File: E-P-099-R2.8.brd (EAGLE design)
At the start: 100 x 80 mm, 86 parts, among them J1 AVR_ISP

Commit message: Gerbers Generated
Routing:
- net GND: track 4.96 -> 15.3 mm, vias 12 -> 17
- net +12V: track 11.4 -> 15.6 mm
- net MISO: track 38.6 -> 41.0 mm
- net N$43: track 23.0 -> 22.2 mm

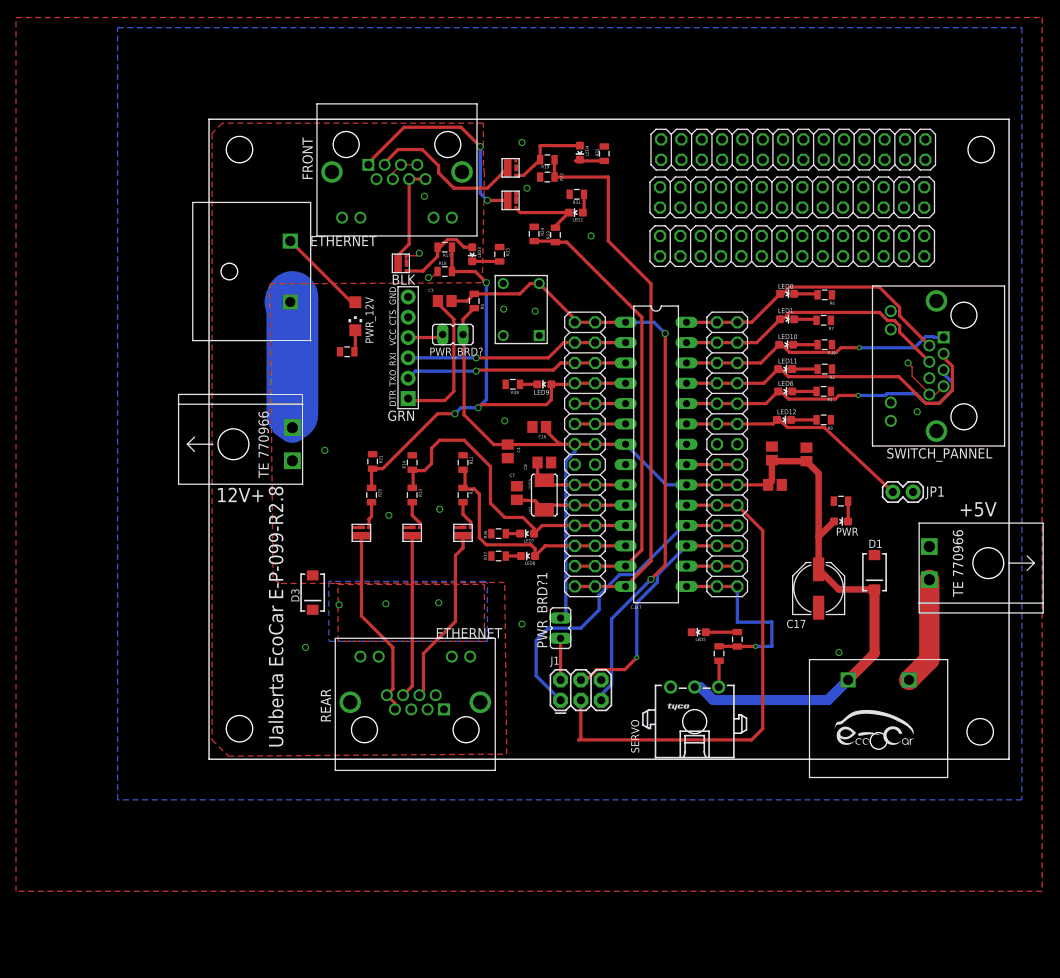
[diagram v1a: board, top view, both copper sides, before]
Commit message: VER.3
Added through hole mosfets, fixed input switch logic, improved pull downs on inout, added connector for break switch,   increased board size and fixed routing,
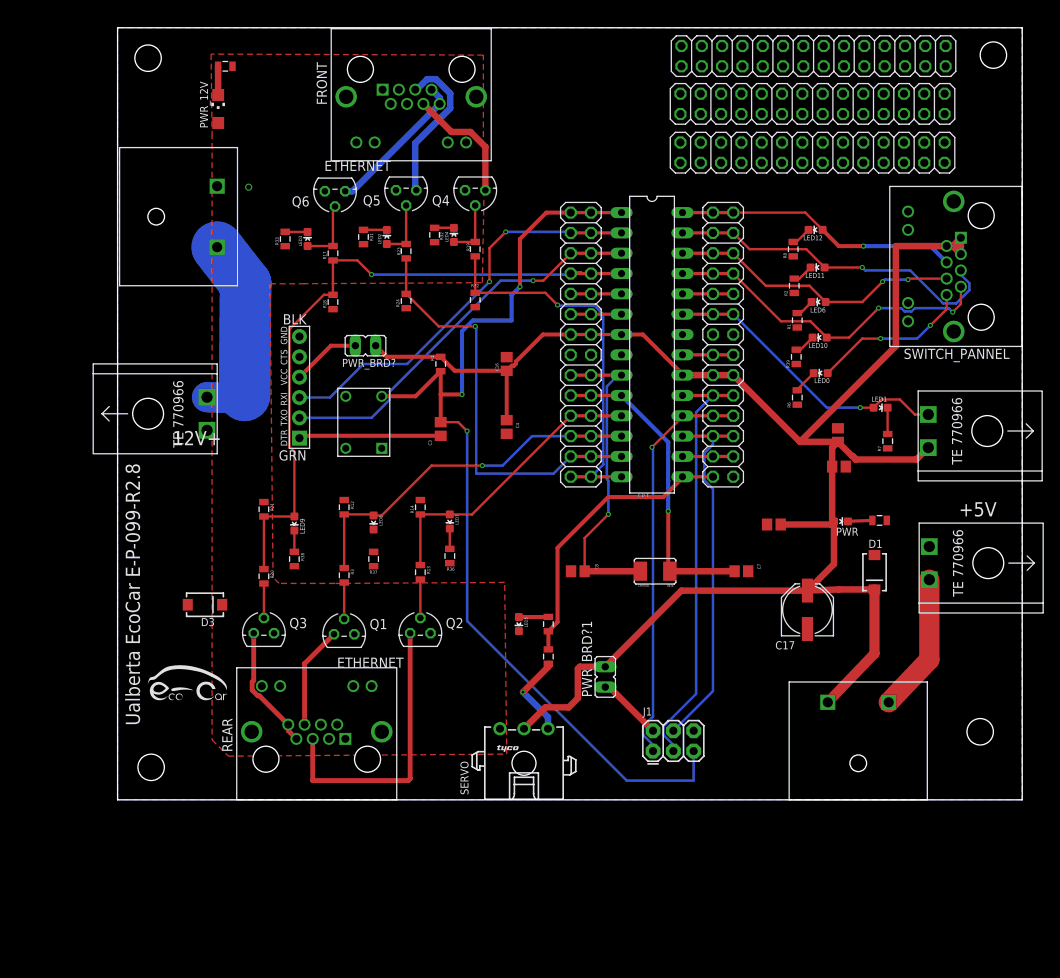
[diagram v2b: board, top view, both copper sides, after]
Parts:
- removed JP1: (no value), SparkFun-Retired:1X02
- removed U$10, U$11, U$13, U$14, U$15, U$20: SIA426DJ, Shell2013:SC70-6L
- added Q1, Q2, Q3, Q4, Q5, Q6: BSS101, transistor-fet:TO92
- added U$3: TE770966, Shell2013(1):2X1-MATE-N-LOCK
- moved R16 38.8 mm to (2.03, 86.6), turned to 0 degrees
- moved LED9 35.8 mm to (10.7, 29.5), turned to 180 degrees
- moved R38 35.0 mm to (10.7, 25.0), turned to 270 degrees
- moved PWR_12V 31.1 mm to (1.14, 81.3), turned to 0 degrees
- moved C7 29.7 mm to (66.5, 23.5), turned to 0 degrees
- moved R31 27.2 mm to (19.3, 65.3), turned to 90 degrees
- moved R33 26.9 mm to (9.53, 65.0), turned to 90 degrees
- moved U$12 24.2 mm to (21.6, 38.9)
- moved LED12 24.1 mm to (75.8, 66.2), turned to 90 degrees
- moved LED2 23.8 mm to (22.2, 65.3), turned to 0 degrees
- moved R34 23.7 mm to (42.4, 16.9)
- moved R32 23.5 mm to (28.2, 65.5), turned to 90 degrees
- moved LED5 22.5 mm to (38.7, 16.9), turned to 180 degrees
- moved SERVO 22.0 mm to (39.4, -0.51)
- moved R8 21.7 mm to (73.0, 63.8), turned to 90 degrees
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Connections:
- removed net N$27: FRONT.P$6, FRONT.P$8, U$10.D
- removed net N$43: REAR.P$4, U$14.D
- removed net N$49: LED2.A, R31.2
- new net N$14: Q2.2, R13.2
- new net N$15: Q1.2, R3.2
- new net N$22: FRONT.P$5, Q5.3
- net +12V: now also FRONT.P$1, FRONT.P$3, REAR.P$4; no longer FRONT.P$5, FRONT.P$7, REAR.P$5
- net +5V: now also SWITCH_PANNEL.P$1, SWITCH_PANNEL.P$2, SWITCH_PANNEL.P$3, U$3.CIRCUIT1
- net BREAK_SWITCH: now also LED1.A, U$3.CIRCUIT2; no longer JP1.1, LED12.A
- net DRIVING_LIGHTS_SWITCH: now also LED6.A, SWITCH_PANNEL.P$6; no longer LED10.A, SWITCH_PANNEL.P$1
- net FREE: now also LED0.A, SWITCH_PANNEL.P$8; no longer SWITCH_PANNEL.P$6
- net GND: now also Q1.1, Q2.1, Q3.1, Q4.1, Q5.1, Q6.1; no longer FRONT.P$13, FRONT.P$14, JP1.2, SWITCH_PANNEL.P$13, SWITCH_PANNEL.P$14, SWITCH_PANNEL.P$7, SWITCH_PANNEL.P$8, U$10.S@0, U$10.S@1, U$11.S@0, U$11.S@1, U$13.S@0, U$13.S@1, U$14.S@0, U$14.S@1, U$15.S@0, U$15.S@1, U$20.S@0, U$20.S@1
- net HAZ_SWITCH: now also LED10.A, SWITCH_PANNEL.P$7; no longer LED11.A, SWITCH_PANNEL.P$3
- net LEFT_SWITCH: now also LED11.A, SWITCH_PANNEL.P$5; no longer LED1.A, SWITCH_PANNEL.P$4
- net N$17: now also LED2.A, Q5.2; no longer LED2.C, U$20.G
- net N$20: now also FRONT.P$7, FRONT.P$8, Q6.3; no longer FRONT.P$1, U$20.D
- net N$21: now also FRONT.P$6, Q4.3; no longer R3.2, U$14.G
- net N$23: now also LED2.C, R31.2; no longer FRONT.P$3, U$11.D
- net N$33: now also Q4.2; no longer U$11.G
- net N$35: now also Q6.2; no longer U$10.G
- net N$4: now also Q3.3; no longer U$13.D
- net N$5: now also Q1.3; no longer U$15.D
- net N$7: now also Q2.3, REAR.P$5; no longer R13.2, U$15.G
- net N$8: now also Q3.2; no longer U$13.G
- net RIGHT_SWITCH: now also LED12.A, SWITCH_PANNEL.P$4; no longer LED0.A, SWITCH_PANNEL.P$2
- net WIPER_SWITCH: no longer LED6.A, SWITCH_PANNEL.P$5
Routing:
- net +5V: track 147.2 -> 227.0 mm
- net RESET: track 79.6 -> 125.5 mm, vias 2 -> 3
- net WIPER_SWITCH: track 38.7 -> 6.35 mm, vias 1 -> 0
- net N$7: track 3.56 -> 35.7 mm
- net XTAL1: track 13.0 -> 40.1 mm, vias 0 -> 1
- net XTAL2: track 14.3 -> 38.9 mm, vias 0 -> 1
- net RX: track 28.0 -> 51.3 mm, vias 1 -> 2
- net N$43: track 22.2 -> 0.00 mm
- net TX: track 28.0 -> 49.4 mm
- net BLINK_R: track 70.1 -> 49.4 mm, vias 0 -> 1
- net DRIVING_LIGHTS: track 63.6 -> 83.7 mm, vias 3 -> 1
- net FREE: track 0.00 -> 20.0 mm, vias 0 -> 2
- net N$22: track 0.00 -> 19.6 mm
- net N$23: track 19.9 -> 2.93 mm
- net +12V: track 15.6 -> 0.00 mm, vias 3 -> 0
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- removed copper zone on layer 16, net +12V
- removed copper zone on layer 1, net GND
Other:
- board size 100 x 80 mm -> 113.1 x 96.5 mm

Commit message: added pull down resistors to switches, added windshield wiper switch, added capacitors to make mike happy, adjusted led circuit on outputs might need different resistor values, changed a couple other things
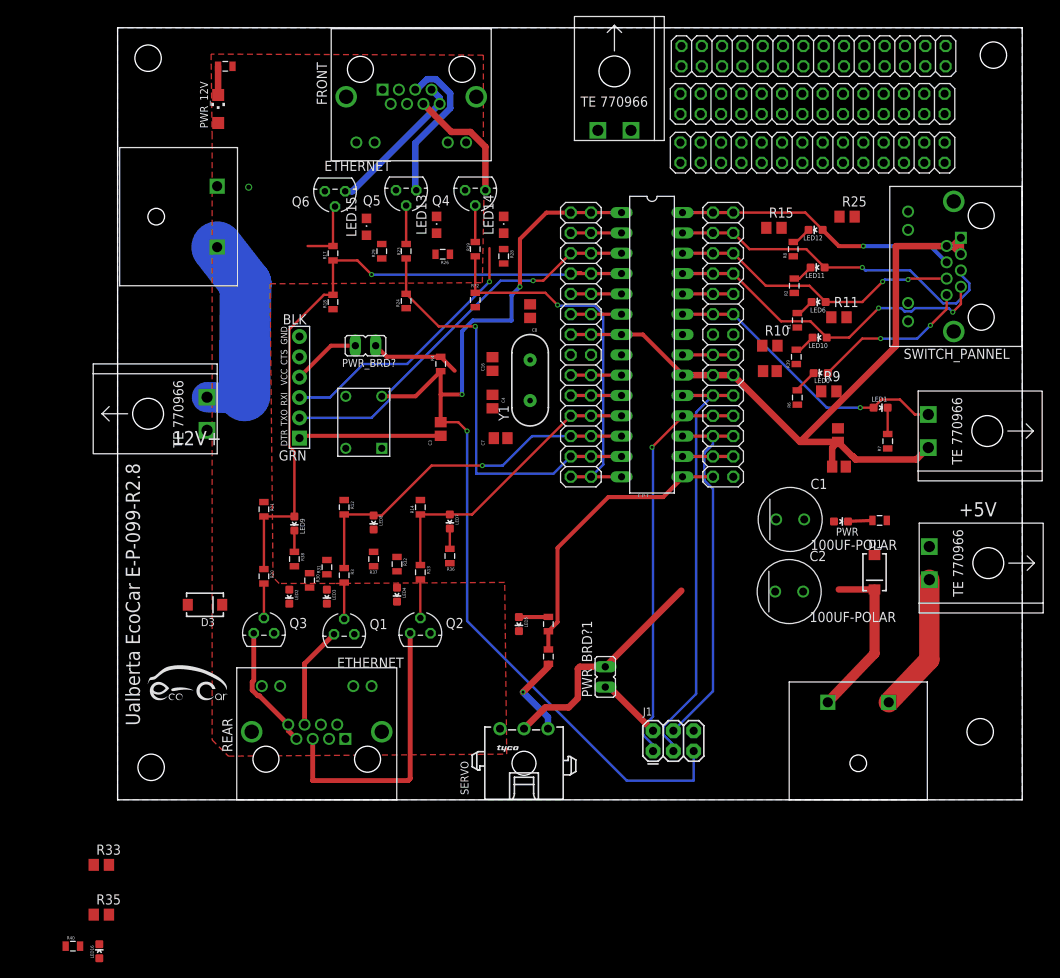
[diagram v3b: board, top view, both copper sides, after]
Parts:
- removed C17: 100uF, SparkFun-Capacitors:PANASONIC_D
- removed U$18: CRYSTAL, mylibrary:7A_CRYSTAL
- added C1, C2: 100UF-POLAR, 100uF_Cap:EEU-FR1H101
- added LED13, LED14, LED15: (no value), led:CHIPLED_0805
- added LED16: (no value), SparkFun-LED:LED-0603
- added R10, R11, R15, R25, R35, R9: 10K, resistor:R0805
- added R26, R28, R29, R40: 1K, SparkFun-Passives:0805
- added R30: 430, SparkFun-Passives:0805
- added U$5: TE770966, Shell2013(1):2X1-MATE-N-LOCK
- added Y1: (no value), SparkFun-FreqCtrl:HC49US
- R31, R32: value 330 -> 430
- R33: value 330 -> 10K; device SparkFun-Passives:0805 -> resistor:R0805
- moved R33 81.5 mm to (-13.5, -13.2), turned to 0 degrees
- moved LED2 46.6 mm to (10.0, 20.3), turned to 180 degrees
- moved LED4 45.5 mm to (23.5, 20.6), turned to 180 degrees
- moved LED3 44.8 mm to (14.7, 20.3), turned to 180 degrees
- moved R31 41.5 mm to (14.7, 24.0)
- moved R32 41.4 mm to (23.5, 24.4), turned to 270 degrees
- moved C7 34.4 mm to (36.4, 40.1), turned to 180 degrees
- moved C8 33.1 mm to (40.1, 56.0), turned to 90 degrees
- moved C14 19.2 mm to (70.1, 48.5)
- moved C4 3.64 mm to (35.4, 44.7)
- moved C16 1.78 mm to (35.4, 49.4)
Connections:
- removed net N$31: LED4.C, R32.2
- removed net N$38: LED3.C, R33.2
- new net N$18: LED4.A, R32.2
- new net N$24: C8.1, Y1.2
- new net N$27: LED2.A, R30.2
- new net N$28: LED16.C, R40.2
- new net N$32: LED13.A, R26.2
- new net N$34: LED14.A, R28.1
- new net N$36: LED15.A, R29.2
- net +12V: now also R26.1, R28.2, R29.1, R30.1, R31.2, R32.1
- net +5V: now also C1.P, C2.P, U$5.CIRCUIT1; no longer C17.+
- net BREAK_SWITCH: now also R35.2
- net DRIVING_LIGHTS_SWITCH: now also R11.2
- net FREE: now also R9.2
- net GND: now also C1.G, C2.G, R10.1, R11.1, R15.1, R25.1, R33.2, R35.1, R40.1, R9.1; no longer C17.-, R31.1, R32.1, R33.1
- net HAZ_SWITCH: now also R10.2
- net LEFT_SWITCH: now also R15.2
- net N$17: no longer LED2.A
- net N$20: now also LED15.C
- net N$21: now also LED14.C
- net N$22: now also LED13.C
- net N$23: now also LED3.A, R31.1; no longer LED2.C, R31.2
- net N$33: no longer LED4.A
- net N$35: no longer LED3.A
- net N$4: now also LED2.C
- net N$5: now also LED3.C
- net N$7: now also LED4.C
- net RIGHT_SWITCH: now also R25.2
- net WIPER_SWITCH: now also LED16.A, R33.1, U$5.CIRCUIT2
- net XTAL1: no longer C8.1, U$18.P$2
- net XTAL2: now also Y1.1; no longer U$18.P$1
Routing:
- net +5V: track 227.0 -> 160.8 mm
- net XTAL1: track 40.1 -> 6.78 mm, vias 1 -> 0
- net XTAL2: track 38.9 -> 6.35 mm, vias 1 -> 0
- net RX: track 51.3 -> 40.5 mm, vias 2 -> 1
- net N$23: track 2.93 -> 0.00 mm
- net N$38: track 2.80 -> 0.00 mm
- net N$33: track 7.23 -> 4.56 mm
- net N$31: track 2.42 -> 0.00 mm
- net N$17: track 7.23 -> 4.82 mm
